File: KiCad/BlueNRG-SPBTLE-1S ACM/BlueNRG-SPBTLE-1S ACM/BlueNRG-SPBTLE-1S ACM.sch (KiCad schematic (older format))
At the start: 12 parts, among them J1 Conn_01x04_Female, U1 LSM6DS3, U2 SPBTLE-1S

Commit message: Added a push button for the RST pin and an IC for the power management
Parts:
- added C6, C7: 1u, Capacitor_SMD:C_0805_2012Metric_Pad1.15x1.40mm_HandSolder, symbol Device:C
- added J2: Conn_01x03, Jumper:SolderJumper-3_P1.3mm_Open_RoundedPad1.0x1.5mm, symbol Connector_Generic:Conn_01x03
- added R3: 100k, Resistor_SMD:R_0805_2012Metric_Pad1.15x1.40mm_HandSolder, symbol Device:R
- added TL3305A1: SW_Push_Dual, Button_Switch_SMD:SW_SPST_TL3305A, symbol Switch:SW_Push_Dual
- added U3: TLV70033_SOT23-5, Package_TO_SOT_SMD:SOT-23-5, symbol Regulator_Linear:TLV70033_SOT23-5
- J1: footprint SPBTLE-1S:JTAG-SWD-4PINS -> Socket_Strips:Socket_Strip_Straight_1x04_Pitch2.00mm
- R2: value 47k -> 100k
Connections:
- wire segments 49 -> 67
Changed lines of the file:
@@
 EESchema Schematic File Version 4
+LIBS:BlueNRG-SPBTLE-1S ACM-cache
 EELAYER 26 0
 EELAYER END
@@
 F 0 "J1" H 2577 3726 50  0000 L CNN
 F 1 "Conn_01x04_Female" H 2577 3635 50  0000 L CNN
-F 2 "SPBTLE-1S:JTAG-SWD-4PINS" H 2550 3750 50  0001 C CNN
+F 2 "Socket_Strips:Socket_Strip_Straight_1x04_Pitch2.00mm" H 2550 3750 50  0001 C CNN
 F 3 "~" H 2550 3750 50  0001 C CNN
 	1    2550 3750
@@
 	1    0    0    -1
 $EndComp
-Text GLabel 3550 2350 1    50   Input ~ 0
+Text GLabel 3650 2350 3    50   Input ~ 0
 Vdd
 $Comp
@@
 P 8600 3200
 F 0 "R2" H 8670 3246 50  0000 L CNN
-F 1 "47k" H 8670 3155 50  0000 L CNN
+F 1 "100k" H 8670 3155 50  0000 L CNN
 F 2 "Resistor_SMD:R_0805_2012Metric_Pad1.15x1.40mm_HandSolder" V 8530 3200 50  0001 C CNN
 F 3 "~" H 8600 3200 50  0001 C CNN
@@
 Wire Wire Line
 	4550 6200 4550 6400
-Text GLabel 1950 3650 0    50   Input ~ 0
+Text GLabel 2100 3950 0    50   Input ~ 0
 JTCK-SWCTK
-Text GLabel 1950 3750 0    50   Input ~ 0
+Text GLabel 2100 3850 0    50   Input ~ 0
 JTMS-SWTDIO
-Text GLabel 1900 3950 0    50   Input ~ 0
+Text GLabel 1850 3650 0    50   Input ~ 0
 Vdd
 $Comp
@@
 	1    0    0    -1
 $EndComp
-Wire Wire Line
-	2350 3650 1950 3650
-Wire Wire Line
-	1950 3750 2350 3750
-Wire Wire Line
-	2350 3850 1250 3850
-Wire Wire Line
-	2350 3950 1900 3950
+$Comp
+L Connector_Generic:Conn_01x03 J2
+U 1 1 5C7EB1F7
+P 3550 2150
+F 0 "J2" V 3516 1962 50  0000 R CNN
+F 1 "Conn_01x03" V 3425 1962 50  0000 R CNN
+F 2 "Jumper:SolderJumper-3_P1.3mm_Open_RoundedPad1.0x1.5mm" H 3550 2150 50  0001 C CNN
+F 3 "~" H 3550 2150 50  0001 C CNN
+	1    3550 2150
+	0    -1   -1   0
+$EndComp
+Text GLabel 3100 2600 2    50   Input ~ 0
+Vdd
+$Comp
+L Regulator_Linear:TLV70033_SOT23-5 U3
+U 1 1 5C7EE612
+P 2600 2700
+F 0 "U3" H 2600 3042 50  0000 C CNN
+F 1 "TLV70033_SOT23-5" H 2600 2951 50  0000 C CNN
+F 2 "Package_TO_SOT_SMD:SOT-23-5" H 2600 3025 50  0001 C CIN
+F 3 "http://www.ti.com/lit/ds/symlink/tlv700.pdf" H 2600 2750 50  0001 C CNN
+	1    2600 2700
+	1    0    0    -1
+$EndComp
+Wire Wire Line
+	3450 2350 2600 2350
+Wire Wire Line
+	2150 2350 2150 2600
+Wire Wire Line
+	2150 2600 2300 2600
+Wire Wire Line
+	3100 2600 3000 2600
+$Comp
+L power:GND #PWR012
+U 1 1 5C7F00B0
+P 2600 3150
+F 0 "#PWR012" H 2600 2900 50  0001 C CNN
+F 1 "GND" H 2605 2977 50  0000 C CNN
+F 2 "" H 2600 3150 50  0001 C CNN
+F 3 "" H 2600 3150 50  0001 C CNN
+	1    2600 3150
+	1    0    0    -1
+$EndComp
+Wire Wire Line
+	2600 3000 2600 3150
+Text GLabel 2150 2700 0    50   Input ~ 0
+Vdd
+Wire Wire Line
+	2300 2700 2150 2700
+$Comp
+L Device:C C7
+U 1 1 5C7F392C
+P 3000 2900
+F 0 "C7" H 3115 2946 50  0000 L CNN
+F 1 "1u" H 3115 2855 50  0000 L CNN
+F 2 "Capacitor_SMD:C_0805_2012Metric_Pad1.15x1.40mm_HandSolder" H 3038 2750 50  0001 C CNN
+F 3 "~" H 3000 2900 50  0001 C CNN
+	1    3000 2900
+	1    0    0    -1
+$EndComp
+$Comp
+L power:GND #PWR013
+U 1 1 5C7F39B4
+P 3000 3150
+F 0 "#PWR013" H 3000 2900 50  0001 C CNN
+F 1 "GND" H 3005 2977 50  0000 C CNN
+F 2 "" H 3000 3150 50  0001 C CNN
+F 3 "" H 3000 3150 50  0001 C CNN
+	1    3000 3150
+	1    0    0    -1
+$EndComp
+Wire Wire Line
+	3000 2600 3000 2750
+Connection ~ 3000 2600
+Wire Wire Line
+	3000 2600 2900 2600
+Wire Wire Line
+	3000 3050 3000 3150
+$Comp
+L Device:C C6
+U 1 1 5C7F5837
+P 2600 2000
+F 0 "C6" H 2715 2046 50  0000 L CNN
+F 1 "1u" H 2715 1955 50  0000 L CNN
+F 2 "Capacitor_SMD:C_0805_2012Metric_Pad1.15x1.40mm_HandSolder" H 2638 1850 50  0001 C CNN
+F 3 "~" H 2600 2000 50  0001 C CNN
+	1    2600 2000
+	1    0    0    -1
+$EndComp
+$Comp
+L power:GND #PWR011
+U 1 1 5C7F58C4
+P 2600 1650
+F 0 "#PWR011" H 2600 1400 50  0001 C CNN
+F 1 "GND" H 2605 1477 50  0000 C CNN
+F 2 "" H 2600 1650 50  0001 C CNN
+F 3 "" H 2600 1650 50  0001 C CNN
+	1    2600 1650
+	-1   0    0    1
+$EndComp
+Wire Wire Line
+	2600 1650 2600 1850
+Wire Wire Line
+	2600 2150 2600 2350
+Connection ~ 2600 2350
+Wire Wire Line
+	2600 2350 2150 2350
+Wire Wire Line
+	1850 3650 2350 3650
+Wire Wire Line
+	2350 3750 1250 3750
+Wire Wire Line
+	1250 3750 1250 3850
+Wire Wire Line
+	2350 3850 2100 3850
+Wire Wire Line
+	2350 3950 2100 3950
+$Comp
+L Switch:SW_Push_Dual TL3305A1
+U 1 1 5C7F3079
+P 9450 3750
+F 0 "TL3305A1" V 9496 3462 50  0000 R CNN
+F 1 "SW_Push_Dual" V 9405 3462 50  0000 R CNN
+F 2 "Button_Switch_SMD:SW_SPST_TL3305A" H 9450 3950 50  0001 C CNN
+F 3 "" H 9450 3950 50  0001 C CNN
+	1    9450 3750
+	0    -1   -1   0
+$EndComp
+Wire Wire Line
+	8600 3550 9450 3550
+Wire Wire Line
+	9450 3550 9650 3550
+Connection ~ 9450 3550
+Wire Wire Line
+	9450 3950 9650 3950
+$Comp
+L Device:R R3
+U 1 1 5C7F6ACD
+P 9650 4250
+F 0 "R3" H 9720 4296 50  0000 L CNN
+F 1 "100k" H 9720 4205 50  0000 L CNN
+F 2 "Resistor_SMD:R_0805_2012Metric_Pad1.15x1.40mm_HandSolder" V 9580 4250 50  0001 C CNN
+F 3 "~" H 9650 4250 50  0001 C CNN
+	1    9650 4250
+	1    0    0    -1
+$EndComp
+$Comp
+L power:GND #PWR014
+U 1 1 5C7F6B3B
+P 9650 4500
+F 0 "#PWR014" H 9650 4250 50  0001 C CNN
+F 1 "GND" H 9655 4327 50  0000 C CNN
+F 2 "" H 9650 4500 50  0001 C CNN
+F 3 "" H 9650 4500 50  0001 C CNN
+	1    9650 4500
+	1    0    0    -1
+$EndComp
+Wire Wire Line
+	9650 3950 9650 4100
+Connection ~ 9650 3950
+Wire Wire Line
+	9650 4400 9650 4500
 $EndSCHEMATC

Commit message: Made the necessary modifications for ACM v2 (circuit logic to Vbat, Vdd to SPTBLE)
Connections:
- wire segments 67 -> 69
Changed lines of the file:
@@
 Wire Wire Line
 	2600 3000 2600 3150
-Text GLabel 2150 2700 0    50   Input ~ 0
-Vdd
 Wire Wire Line
 	2300 2700 2150 2700
@@
 Wire Wire Line
 	9650 4400 9650 4500
+Text GLabel 4250 3850 1    50   Input ~ 0
+Vdd
+Wire Wire Line
+	4250 3850 4250 4200
+Wire Wire Line
+	2150 2700 2150 2600
+Connection ~ 2150 2600
 $EndSCHEMATC

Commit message: The first version is completed
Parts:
- removed U2: SPBTLE-1S, SPBTLE-1S:SPBTLE-1S, symbol Custom~Library:SPBTLE-1S
- added U2: SPBTLE-1S-Custom_Library, symbol BlueNRG-SPBTLE-1S-ACM-rescue:SPBTLE-1S-Custom_Library
- U1: symbol LSM6DS3:LSM6DS3 -> BlueNRG-SPBTLE-1S-ACM-rescue:LSM6DS3-LSM6DS3
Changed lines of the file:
@@
 EESchema Schematic File Version 4
 LIBS:BlueNRG-SPBTLE-1S ACM-cache
-EELAYER 26 0
+EELAYER 29 0
 EELAYER END
 $Descr A4 11693 8268
@@
 $EndDescr
 $Comp
-L LSM6DS3:LSM6DS3 U1
+L BlueNRG-SPBTLE-1S-ACM-rescue:LSM6DS3-LSM6DS3 U1
 U 1 1 5C7C28DD
 P 2650 6100
@@
 $EndComp
 $Comp
-L Custom~Library:SPBTLE-1S U2
-U 1 1 5C7C2BC4
-P 5900 3850
-F 0 "U2" H 5875 4728 50  0000 C CNN
-F 1 "SPBTLE-1S" H 5875 4637 50  0000 C CNN
-F 2 "SPBTLE-1S:SPBTLE-1S" H 5550 3750 50  0001 C CNN
-F 3 "" H 5550 3750 50  0001 C CNN
-	1    5900 3850
-	1    0    0    -1
-$EndComp
-$Comp
 L Connector:Conn_01x04_Female J1
 U 1 1 5C7C2CC4
@@
 Wire Wire Line
 	3550 2850 3550 3050
-NoConn ~ 5850 3150
-NoConn ~ 5650 3150
-NoConn ~ 5450 3150
 Text GLabel 6450 4800 3    50   Input ~ 0
 JTMS-SWTDIO
 Text GLabel 6250 4800 3    50   Input ~ 0
 JTCK-SWCTK
-Wire Wire Line
-	6450 4500 6450 4800
-Wire Wire Line
-	6250 4500 6250 4800
-NoConn ~ 6650 4500
-NoConn ~ 5650 4500
 $Comp
 L power:GND #PWR09
@@
 	1    0    0    -1
 $EndComp
-Wire Wire Line
-	5450 4500 5450 4700
 $Comp
 L Device:LED D1
@@
 $EndComp
 Wire Wire Line
-	5250 4500 5250 4700
-Wire Wire Line
 	5250 5000 5250 5150
 Wire Wire Line
 	5250 5450 5250 5650
-NoConn ~ 5050 4500
-NoConn ~ 5850 4500
 $Comp
 L Device:C C1
@@
 $EndComp
 Wire Wire Line
-	4650 4200 4250 4200
-Wire Wire Line
 	3800 4200 3800 4250
 Wire Wire Line
@@
 	3800 4550 4250 4550
 Connection ~ 3800 4550
-NoConn ~ 4650 3800
-NoConn ~ 4650 4000
-NoConn ~ 4650 3400
-NoConn ~ 4650 3600
 Text GLabel 7450 4150 2    50   Input ~ 0
 SPI_CLK
-Wire Wire Line
-	7450 4150 7100 4150
 Text GLabel 7450 3700 2    50   Input ~ 0
 SPI_CS
-NoConn ~ 6050 4500
-Wire Wire Line
-	7450 3700 7100 3700
 Text GLabel 7450 3400 2    50   Input ~ 0
 DIO12-INT
-Wire Wire Line
-	7450 3400 7100 3400
 $Comp
 L Device:C C5
@@
 Wire Wire Line
 	8600 3850 8600 4100
-Wire Wire Line
-	7100 3550 8600 3550
 Connection ~ 8600 3550
 Text GLabel 7450 3850 2    50   Input ~ 0
@@
 Text GLabel 7450 4000 2    50   Input ~ 0
 SPI_OUT
-Wire Wire Line
-	7450 3850 7100 3850
-Wire Wire Line
-	7450 4000 7100 4000
 Text GLabel 1300 6000 0    50   Input ~ 0
 SPI_OUT
@@
 	2150 2700 2150 2600
 Connection ~ 2150 2600
+$Comp
+L BlueNRG-SPBTLE-1S-ACM-rescue:SPBTLE-1S-Custom_Library U2
+U 1 1 5CD1E063
+P 5900 3850
+F 0 "U2" H 5875 4731 50  0000 C CNN
+F 1 "SPBTLE-1S-Custom_Library" H 5875 4640 50  0000 C CNN
+F 2 "" H 5550 3750 50  0001 C CNN
+F 3 "" H 5550 3750 50  0001 C CNN
+	1    5900 3850
+	1    0    0    -1
+$EndComp
+Wire Wire Line
+	4250 4200 4650 4200
+Wire Wire Line
+	5250 4500 5250 4700
+Wire Wire Line
+	6250 4500 6250 4800
+Wire Wire Line
+	6450 4500 6450 4800
+Wire Wire Line
+	7100 4150 7450 4150
+Wire Wire Line
+	7450 4000 7100 4000
+Wire Wire Line
+	7100 3850 7450 3850
+Wire Wire Line
+	7450 3700 7100 3700
+Wire Wire Line
+	7100 3550 8600 3550
+Wire Wire Line
+	7450 3400 7100 3400
+NoConn ~ 5850 3150
+NoConn ~ 5650 3150
+NoConn ~ 5450 3150
+NoConn ~ 4650 3400
+NoConn ~ 4650 3600
+NoConn ~ 4650 3800
+NoConn ~ 4650 4000
+NoConn ~ 5050 4500
+NoConn ~ 5650 4500
+NoConn ~ 5850 4500
+NoConn ~ 6050 4500
+Wire Wire Line
+	5450 4500 5450 4700
+NoConn ~ 6650 4500
 $EndSCHEMATC

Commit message: Added charging capabilities to ACM PCB and removed the screws. Removed the screws from the cover
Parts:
- removed BT1: Battery_Cell, Battery:BatteryHolder_MPD_BC2003_1x2032, symbol Device:Battery_Cell
- removed J2: Conn_01x03, Jumper:SolderJumper-3_P1.3mm_Open_RoundedPad1.0x1.5mm, symbol Connector_Generic:Conn_01x03
- added C8: 1u, Capacitor_SMD:C_0603_1608Metric_Pad1.05x0.95mm_HandSolder, symbol Device:C
- added C9: 4.7u, Capacitor_SMD:C_0603_1608Metric_Pad1.05x0.95mm_HandSolder, symbol Device:C
- added D2, D3: LED, LED_SMD:LED_0805_2012Metric_Pad1.15x1.40mm_HandSolder, symbol Device:LED
- added J2: USB_B_Micro, Connector_USB:USB_Micro-B_Molex-105017-0001, symbol Connector:USB_B_Micro
- added J3: Conn_01x02_Female, Connector_JST:JST_SH_SM02B-SRSS-TB_1x02-1MP_P1.00mm_Horizontal, symbol Connector:Conn_01x02_Female
- added R10: 3.57k, Resistor_SMD:R_0603_1608Metric_Pad1.05x0.95mm_HandSolder, symbol Device:R
- added R4: 56.2k, Resistor_SMD:R_0603_1608Metric_Pad1.05x0.95mm_HandSolder, symbol Device:R
- added R5: 2.94k, Resistor_SMD:R_0603_1608Metric_Pad1.05x0.95mm_HandSolder, symbol Device:R
- added R6: 4.32k, Resistor_SMD:R_0603_1608Metric_Pad1.05x0.95mm_HandSolder, symbol Device:R
- added R7: 10k, Resistor_SMD:R_0603_1608Metric_Pad1.05x0.95mm_HandSolder, symbol Device:R
- added R8, R9: 2k, Resistor_SMD:R_0603_1608Metric_Pad1.05x0.95mm_HandSolder, symbol Device:R
- added U4: BQ24232, Package_DFN_QFN:VQFN-16-1EP_3x3mm_P0.5mm_EP1.68x1.68mm_ThermalVias, symbol crumpschemes:BQ24232
- C1, C2, C3, C4, C5, C6, C7: footprint Capacitor_SMD:C_0805_2012Metric_Pad1.15x1.40mm_HandSolder -> Capacitor_SMD:C_0603_1608Metric_Pad1.05x0.95mm_HandSolder
- R1, R2, R3: footprint Resistor_SMD:R_0805_2012Metric_Pad1.15x1.40mm_HandSolder -> Resistor_SMD:R_0603_1608Metric_Pad1.05x0.95mm_HandSolder
- U2: footprint (none) -> SPBTLE-1S:SPBTLE-1S
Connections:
- net labels added: VOUT_BQ
- wire segments 69 -> 104
- no-connect marks 14 -> 17

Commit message: Modified the charging feature
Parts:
- U1: symbol BlueNRG-SPBTLE-1S-ACM-rescue:LSM6DS3-LSM6DS3 -> BlueNRG-SPBTLE-1S-ACM-rescue:LSM6DS3-LSM6DS3-BlueNRG-SPBTLE-1S-ACM-rescue
- U2: symbol BlueNRG-SPBTLE-1S-ACM-rescue:SPBTLE-1S-Custom_Library -> BlueNRG-SPBTLE-1S-ACM-rescue:SPBTLE-1S-Custom_Library-BlueNRG-SPBTLE-1S-ACM-rescue
- U4: symbol crumpschemes:BQ24232 -> BlueNRG-SPBTLE-1S-ACM-rescue:BQ24232-crumpschemes

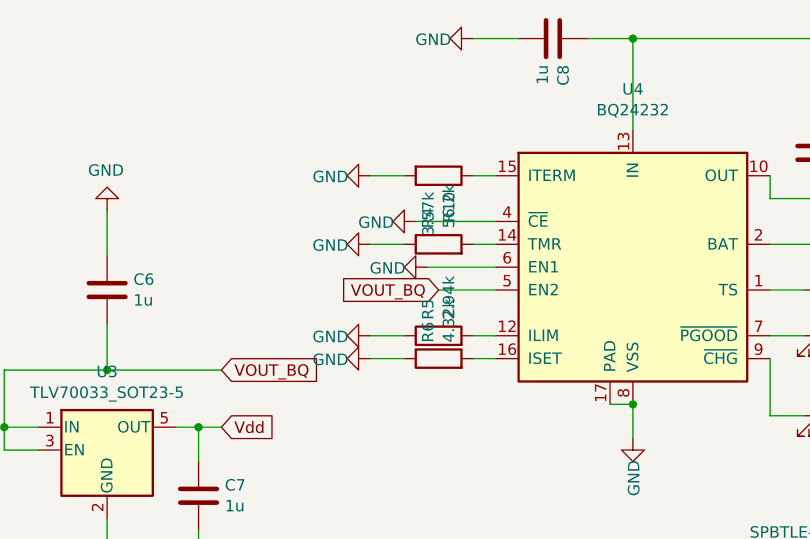
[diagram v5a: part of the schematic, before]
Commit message: Fixed the PCB layout and schematic for the charger U
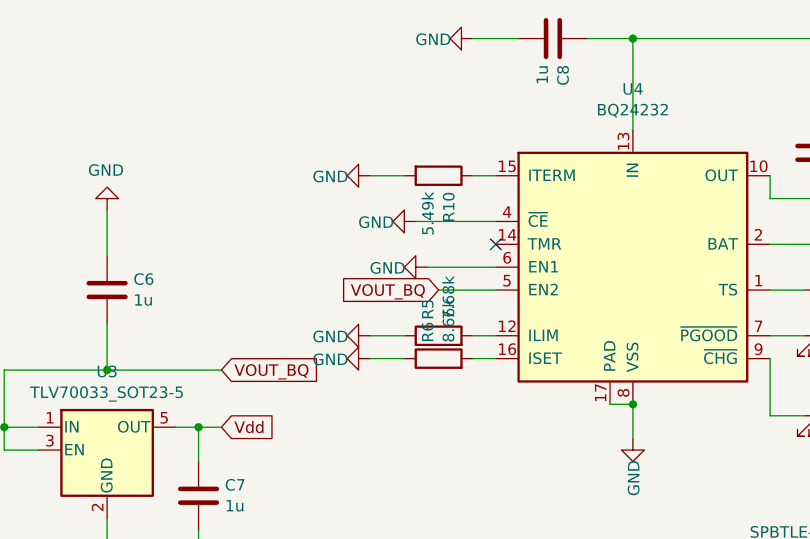
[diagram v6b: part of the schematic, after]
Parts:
- removed R4: 56.2k, Resistor_SMD:R_0603_1608Metric_Pad1.05x0.95mm_HandSolder, symbol Device:R
- R10: value 3.57k -> 5.49k
- R5: value 2.94k -> 7.68k
- R6: value 4.32k -> 8.66k
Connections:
- no-connect marks 17 -> 18
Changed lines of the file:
@@
 EESchema Schematic File Version 4
 LIBS:BlueNRG-SPBTLE-1S ACM-cache
-EELAYER 29 0
+EELAYER 26 0
 EELAYER END
 $Descr A4 11693 8268
@@
 P 4050 1500
 F 0 "R10" H 4120 1546 50  0000 L CNN
-F 1 "3.57k" H 4120 1455 50  0000 L CNN
+F 1 "5.49k" H 4120 1455 50  0000 L CNN
 F 2 "Resistor_SMD:R_0603_1608Metric_Pad1.05x0.95mm_HandSolder" V 3980 1500 50  0001 C CNN
 F 3 "~" H 4050 1500 50  0001 C CNN
@@
 	4200 2200 4300 2200
 Wire Wire Line
-	4200 1800 4300 1800
-Wire Wire Line
 	3750 2300 3900 2300
 Wire Wire Line
 	3750 2200 3900 2200
-Wire Wire Line
-	3750 1800 3900 1800
 $Comp
 L power:GND #PWR0110
@@
 $EndComp
 $Comp
-L power:GND #PWR0108
-U 1 1 5D127FCE
-P 3750 1800
-F 0 "#PWR0108" H 3750 1550 50  0001 C CNN
-F 1 "GND" V 3755 1627 50  0000 C CNN
-F 2 "" H 3750 1800 50  0001 C CNN
-F 3 "" H 3750 1800 50  0001 C CNN
-	1    3750 1800
-	0    1    1    0
-$EndComp
-$Comp
 L Device:R R6
 U 1 1 5D125C10
 P 4050 2300
 F 0 "R6" H 4120 2346 50  0000 L CNN
-F 1 "4.32k" H 4120 2255 50  0000 L CNN
+F 1 "8.66k" H 4120 2255 50  0000 L CNN
 F 2 "Resistor_SMD:R_0603_1608Metric_Pad1.05x0.95mm_HandSolder" V 3980 2300 50  0001 C CNN
 F 3 "~" H 4050 2300 50  0001 C CNN
@@
 P 4050 2200
 F 0 "R5" H 4120 2246 50  0000 L CNN
-F 1 "2.94k" H 4120 2155 50  0000 L CNN
+F 1 "7.68k" H 4120 2155 50  0000 L CNN
 F 2 "Resistor_SMD:R_0603_1608Metric_Pad1.05x0.95mm_HandSolder" V 3980 2200 50  0001 C CNN
 F 3 "~" H 4050 2200 50  0001 C CNN
 	1    4050 2200
-	0    -1   -1   0
-$EndComp
-$Comp
-L Device:R R4
-U 1 1 5D125B2C
-P 4050 1800
-F 0 "R4" H 4120 1846 50  0000 L CNN
-F 1 "56.2k" H 4120 1755 50  0000 L CNN
-F 2 "Resistor_SMD:R_0603_1608Metric_Pad1.05x0.95mm_HandSolder" V 3980 1800 50  0001 C CNN
-F 3 "~" H 4050 1800 50  0001 C CNN
-	1    4050 1800
 	0    -1   -1   0
 $EndComp
@@
 $EndComp
 Wire Wire Line
-	4300 2000 4050 2000
-Text GLabel 4050 2000 0    50   Input ~ 0
-VOUT_BQ
-Wire Wire Line
 	5700 1600 5950 1600
 Wire Wire Line
@@
 Wire Wire Line
 	5500 2000 5650 2000
-$Comp
-L power:GND #PWR0104
-U 1 1 5D0FBFA1
-P 6050 2000
-F 0 "#PWR0104" H 6050 1750 50  0001 C CNN
-F 1 "GND" H 6055 1827 50  0000 C CNN
-F 2 "" H 6050 2000 50  0001 C CNN
-F 3 "" H 6050 2000 50  0001 C CNN
-	1    6050 2000
-	0    -1   -1   0
-$EndComp
 $Comp
 L Device:R R7
@@
 	1    0    0    -1
 $EndComp
+$Comp
+L power:GND #PWR0104
+U 1 1 5D0FBFA1
+P 6050 2000
+F 0 "#PWR0104" H 6050 1750 50  0001 C CNN
+F 1 "GND" H 6055 1827 50  0000 C CNN
+F 2 "" H 6050 2000 50  0001 C CNN
+F 3 "" H 6050 2000 50  0001 C CNN
+	1    6050 2000
+	0    -1   -1   0
+$EndComp
+Wire Wire Line
+	4300 2000 4050 2000
+Text GLabel 4050 2000 0    50   Input ~ 0
+VOUT_BQ
+NoConn ~ 4300 1800
 $EndSCHEMATC
